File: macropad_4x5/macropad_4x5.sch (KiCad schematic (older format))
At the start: 41 parts

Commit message: Update to THT diodes
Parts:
- D1, D10, D11, D12, D13, D14, D15, D16, D17, D18, D19, D2, D20, D3, D4, D5, D6, D7, D8, D9: footprint Diode_SMD:D_SOD-123 -> Diode_THT:D_A-405_P7.62mm_Horizontal
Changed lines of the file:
@@
 F 0 "D1" H 3950 1950 50  0000 R CNN
 F 1 "D_Small" H 4100 2050 50  0000 R CNN
-F 2 "Diode_SMD:D_SOD-123" V 3900 1850 50  0001 C CNN
+F 2 "Diode_THT:D_A-405_P7.62mm_Horizontal" V 3900 1850 50  0001 C CNN
 F 3 "~" V 3900 1850 50  0001 C CNN
 	1    3900 1850
@@
 F 0 "D5" H 3950 2700 50  0000 R CNN
 F 1 "D_Small" H 4150 2800 50  0000 R CNN
-F 2 "Diode_SMD:D_SOD-123" V 3900 2600 50  0001 C CNN
+F 2 "Diode_THT:D_A-405_P7.62mm_Horizontal" V 3900 2600 50  0001 C CNN
 F 3 "~" V 3900 2600 50  0001 C CNN
 	1    3900 2600
@@
 F 0 "D9" H 3950 3450 50  0000 R CNN
 F 1 "D_Small" H 4150 3550 50  0000 R CNN
-F 2 "Diode_SMD:D_SOD-123" V 3900 3350 50  0001 C CNN
+F 2 "Diode_THT:D_A-405_P7.62mm_Horizontal" V 3900 3350 50  0001 C CNN
 F 3 "~" V 3900 3350 50  0001 C CNN
 	1    3900 3350
@@
 F 0 "D13" H 3950 4200 50  0000 R CNN
 F 1 "D_Small" H 4150 4300 50  0000 R CNN
-F 2 "Diode_SMD:D_SOD-123" V 3900 4100 50  0001 C CNN
+F 2 "Diode_THT:D_A-405_P7.62mm_Horizontal" V 3900 4100 50  0001 C CNN
 F 3 "~" V 3900 4100 50  0001 C CNN
 	1    3900 4100
@@
 F 0 "D17" H 3950 4950 50  0000 R CNN
 F 1 "D_Small" H 4150 5050 50  0000 R CNN
-F 2 "Diode_SMD:D_SOD-123" V 3900 4850 50  0001 C CNN
+F 2 "Diode_THT:D_A-405_P7.62mm_Horizontal" V 3900 4850 50  0001 C CNN
 F 3 "~" V 3900 4850 50  0001 C CNN
 	1    3900 4850
@@
 F 0 "D20" H 6950 4950 50  0000 R CNN
 F 1 "D_Small" H 7150 5050 50  0000 R CNN
-F 2 "Diode_SMD:D_SOD-123" V 6900 4850 50  0001 C CNN
+F 2 "Diode_THT:D_A-405_P7.62mm_Horizontal" V 6900 4850 50  0001 C CNN
 F 3 "~" V 6900 4850 50  0001 C CNN
 	1    6900 4850
@@
 F 0 "D19" H 5950 4950 50  0000 R CNN
 F 1 "D_Small" H 6150 5050 50  0000 R CNN
-F 2 "Diode_SMD:D_SOD-123" V 5900 4850 50  0001 C CNN
+F 2 "Diode_THT:D_A-405_P7.62mm_Horizontal" V 5900 4850 50  0001 C CNN
 F 3 "~" V 5900 4850 50  0001 C CNN
 	1    5900 4850
@@
 F 0 "D18" H 4950 4950 50  0000 R CNN
 F 1 "D_Small" H 5150 5050 50  0000 R CNN
-F 2 "Diode_SMD:D_SOD-123" V 4900 4850 50  0001 C CNN
+F 2 "Diode_THT:D_A-405_P7.62mm_Horizontal" V 4900 4850 50  0001 C CNN
 F 3 "~" V 4900 4850 50  0001 C CNN
 	1    4900 4850
@@
 F 0 "D16" H 6950 4200 50  0000 R CNN
 F 1 "D_Small" H 7150 4300 50  0000 R CNN
-F 2 "Diode_SMD:D_SOD-123" V 6900 4100 50  0001 C CNN
+F 2 "Diode_THT:D_A-405_P7.62mm_Horizontal" V 6900 4100 50  0001 C CNN
 F 3 "~" V 6900 4100 50  0001 C CNN
 	1    6900 4100
@@
 F 0 "D15" H 5950 4200 50  0000 R CNN
 F 1 "D_Small" H 6150 4300 50  0000 R CNN
-F 2 "Diode_SMD:D_SOD-123" V 5900 4100 50  0001 C CNN
+F 2 "Diode_THT:D_A-405_P7.62mm_Horizontal" V 5900 4100 50  0001 C CNN
 F 3 "~" V 5900 4100 50  0001 C CNN
 	1    5900 4100
@@
 F 0 "D14" H 4950 4200 50  0000 R CNN
 F 1 "D_Small" H 5150 4300 50  0000 R CNN
-F 2 "Diode_SMD:D_SOD-123" V 4900 4100 50  0001 C CNN
+F 2 "Diode_THT:D_A-405_P7.62mm_Horizontal" V 4900 4100 50  0001 C CNN
 F 3 "~" V 4900 4100 50  0001 C CNN
 	1    4900 4100
@@
 F 0 "D12" H 6950 3450 50  0000 R CNN
 F 1 "D_Small" H 7150 3550 50  0000 R CNN
-F 2 "Diode_SMD:D_SOD-123" V 6900 3350 50  0001 C CNN
+F 2 "Diode_THT:D_A-405_P7.62mm_Horizontal" V 6900 3350 50  0001 C CNN
 F 3 "~" V 6900 3350 50  0001 C CNN
 	1    6900 3350
@@
 F 0 "D11" H 5950 3450 50  0000 R CNN
 F 1 "D_Small" H 6150 3550 50  0000 R CNN
-F 2 "Diode_SMD:D_SOD-123" V 5900 3350 50  0001 C CNN
+F 2 "Diode_THT:D_A-405_P7.62mm_Horizontal" V 5900 3350 50  0001 C CNN
 F 3 "~" V 5900 3350 50  0001 C CNN
 	1    5900 3350
@@
 F 0 "D10" H 4950 3450 50  0000 R CNN
 F 1 "D_Small" H 5150 3550 50  0000 R CNN
-F 2 "Diode_SMD:D_SOD-123" V 4900 3350 50  0001 C CNN
+F 2 "Diode_THT:D_A-405_P7.62mm_Horizontal" V 4900 3350 50  0001 C CNN
 F 3 "~" V 4900 3350 50  0001 C CNN
 	1    4900 3350
@@
 F 0 "D8" H 6950 2700 50  0000 R CNN
 F 1 "D_Small" H 7150 2800 50  0000 R CNN
-F 2 "Diode_SMD:D_SOD-123" V 6900 2600 50  0001 C CNN
+F 2 "Diode_THT:D_A-405_P7.62mm_Horizontal" V 6900 2600 50  0001 C CNN
 F 3 "~" V 6900 2600 50  0001 C CNN
 	1    6900 2600
@@
 F 0 "D7" H 5950 2700 50  0000 R CNN
 F 1 "D_Small" H 6150 2800 50  0000 R CNN
-F 2 "Diode_SMD:D_SOD-123" V 5900 2600 50  0001 C CNN
+F 2 "Diode_THT:D_A-405_P7.62mm_Horizontal" V 5900 2600 50  0001 C CNN
 F 3 "~" V 5900 2600 50  0001 C CNN
 	1    5900 2600
@@
 F 0 "D6" H 4950 2700 50  0000 R CNN
 F 1 "D_Small" H 5150 2800 50  0000 R CNN
-F 2 "Diode_SMD:D_SOD-123" V 4900 2600 50  0001 C CNN
+F 2 "Diode_THT:D_A-405_P7.62mm_Horizontal" V 4900 2600 50  0001 C CNN
 F 3 "~" V 4900 2600 50  0001 C CNN
 	1    4900 2600
@@
 F 0 "D4" H 6950 1950 50  0000 R CNN
 F 1 "D_Small" H 7150 2050 50  0000 R CNN
-F 2 "Diode_SMD:D_SOD-123" V 6900 1850 50  0001 C CNN
+F 2 "Diode_THT:D_A-405_P7.62mm_Horizontal" V 6900 1850 50  0001 C CNN
 F 3 "~" V 6900 1850 50  0001 C CNN
 	1    6900 1850
@@
 F 0 "D3" H 5950 1950 50  0000 R CNN
 F 1 "D_Small" H 6150 2050 50  0000 R CNN
-F 2 "Diode_SMD:D_SOD-123" V 5900 1850 50  0001 C CNN
+F 2 "Diode_THT:D_A-405_P7.62mm_Horizontal" V 5900 1850 50  0001 C CNN
 F 3 "~" V 5900 1850 50  0001 C CNN
 	1    5900 1850
@@
 F 0 "D2" H 4950 1950 50  0000 R CNN
 F 1 "D_Small" H 5100 2050 50  0000 R CNN
-F 2 "Diode_SMD:D_SOD-123" V 4900 1850 50  0001 C CNN
+F 2 "Diode_THT:D_A-405_P7.62mm_Horizontal" V 4900 1850 50  0001 C CNN
 F 3 "~" V 4900 1850 50  0001 C CNN
 	1    4900 1850

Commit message: Updated schematic and pcb routing
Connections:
- net col0: now also B1.20 (A3); no longer B1.17 (A0)
- net col1: now also B1.19 (A2); no longer B1.18 (A1)
- net col2: now also B1.17 (A0); no longer B1.19 (A2)
- net col3: now also B1.18 (A1); no longer B1.20 (A3)
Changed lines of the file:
@@
 Text GLabel 3450 4950 0    50   Input ~ 0
 row4
+Text GLabel 2100 3100 2    50   Input ~ 0
+col0
+Text GLabel 2100 3200 2    50   Input ~ 0
+col1
 Text GLabel 2100 3400 2    50   Input ~ 0
-col0
+col2
 Text GLabel 2100 3300 2    50   Input ~ 0
-col1
-Text GLabel 2100 3200 2    50   Input ~ 0
-col2
-Text GLabel 2100 3100 2    50   Input ~ 0
 col3
 Text GLabel 1200 3100 0    50   Input ~ 0

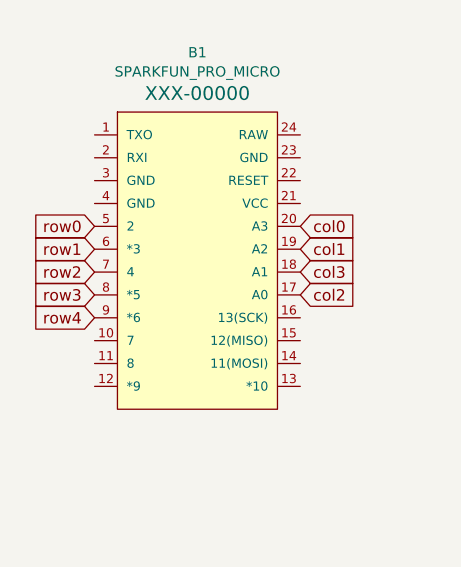
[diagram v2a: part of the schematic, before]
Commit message: Updated schematics and pcb design to clean it up
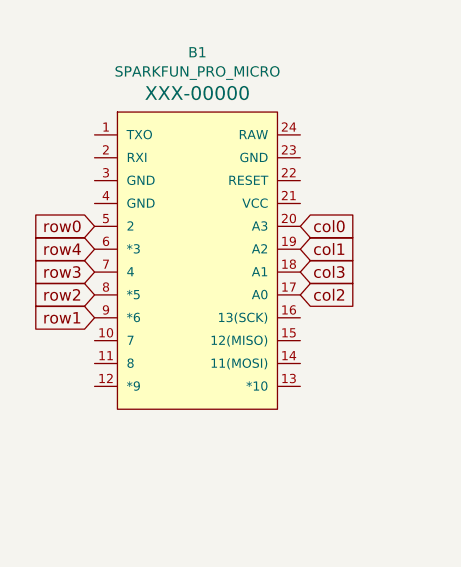
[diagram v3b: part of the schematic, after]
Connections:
- net row1: now also B1.9 (*6); no longer B1.6 (*3)
- net row2: now also B1.8 (*5); no longer B1.7 (4)
- net row3: now also B1.7 (4); no longer B1.8 (*5)
- net row4: now also B1.6 (*3); no longer B1.9 (*6)
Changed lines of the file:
@@
 Text GLabel 1200 3100 0    50   Input ~ 0
 row0
+Text GLabel 1200 3500 0    50   Input ~ 0
+row1
+Text GLabel 1200 3400 0    50   Input ~ 0
+row2
+Text GLabel 1200 3300 0    50   Input ~ 0
+row3
 Text GLabel 1200 3200 0    50   Input ~ 0
-row1
-Text GLabel 1200 3300 0    50   Input ~ 0
-row2
-Text GLabel 1200 3400 0    50   Input ~ 0
-row3
-Text GLabel 1200 3500 0    50   Input ~ 0
 row4
 $EndSCHEMATC

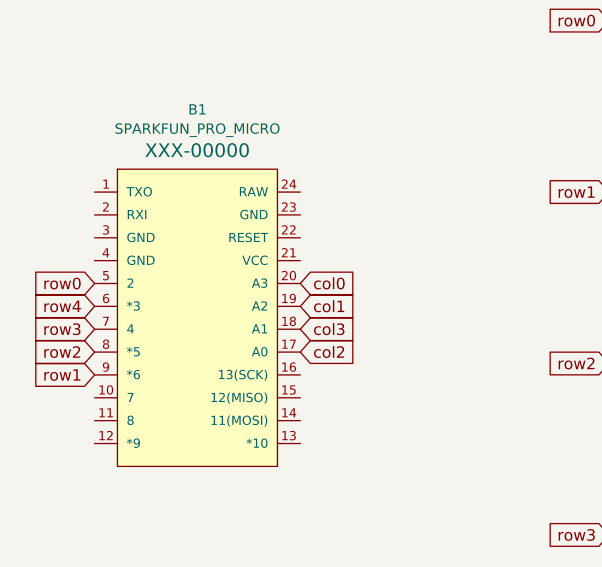
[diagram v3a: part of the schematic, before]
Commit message: Updated PCB
The pro micro was facing the wrong way previously. Also added more text
to the silk layers to help marking for use.
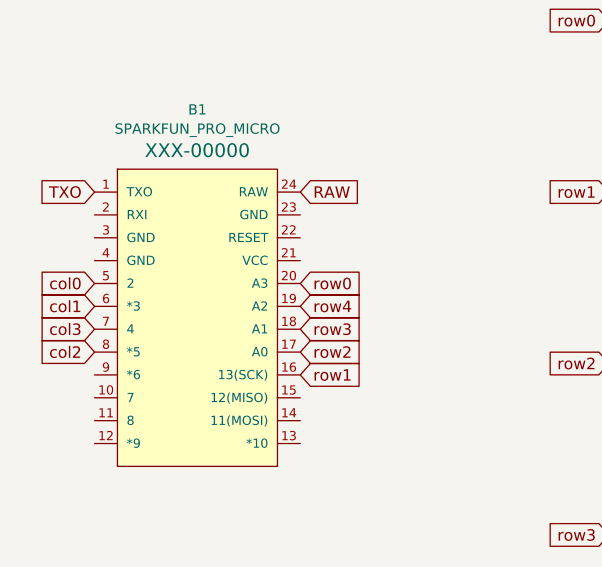
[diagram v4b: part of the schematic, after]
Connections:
- net col0: now also B1.5 (2); no longer B1.20 (A3)
- net col1: now also B1.6 (*3); no longer B1.19 (A2)
- net col2: now also B1.8 (*5); no longer B1.17 (A0)
- net col3: now also B1.7 (4); no longer B1.18 (A1)
- net row0: now also B1.20 (A3); no longer B1.5 (2)
- net row1: now also B1.16 (13(SCK)); no longer B1.9 (*6)
- net row2: now also B1.17 (A0); no longer B1.8 (*5)
- net row3: now also B1.18 (A1); no longer B1.7 (4)
- net row4: now also B1.19 (A2); no longer B1.6 (*3)
- net TXO: now reaches B1.1 (TXO)
- net RAW: now reaches B1.24 (RAW)
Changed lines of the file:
@@
 Text GLabel 3450 4950 0    50   Input ~ 0
 row4
+Text GLabel 1200 3100 0    50   Input ~ 0
+col0
+Text GLabel 1200 3200 0    50   Input ~ 0
+col1
+Text GLabel 1200 3400 0    50   Input ~ 0
+col2
+Text GLabel 1200 3300 0    50   Input ~ 0
+col3
 Text GLabel 2100 3100 2    50   Input ~ 0
-col0
+row0
+Text GLabel 2100 3500 2    50   Input ~ 0
+row1
+Text GLabel 2100 3400 2    50   Input ~ 0
+row2
+Text GLabel 2100 3300 2    50   Input ~ 0
+row3
 Text GLabel 2100 3200 2    50   Input ~ 0
-col1
-Text GLabel 2100 3400 2    50   Input ~ 0
-col2
-Text GLabel 2100 3300 2    50   Input ~ 0
-col3
-Text GLabel 1200 3100 0    50   Input ~ 0
-row0
-Text GLabel 1200 3500 0    50   Input ~ 0
-row1
-Text GLabel 1200 3400 0    50   Input ~ 0
-row2
-Text GLabel 1200 3300 0    50   Input ~ 0
-row3
-Text GLabel 1200 3200 0    50   Input ~ 0
 row4
+Text GLabel 2100 2700 2    50   Input ~ 0
+RAW
+Text GLabel 1200 2700 0    50   Input ~ 0
+TXO
 $EndSCHEMATC

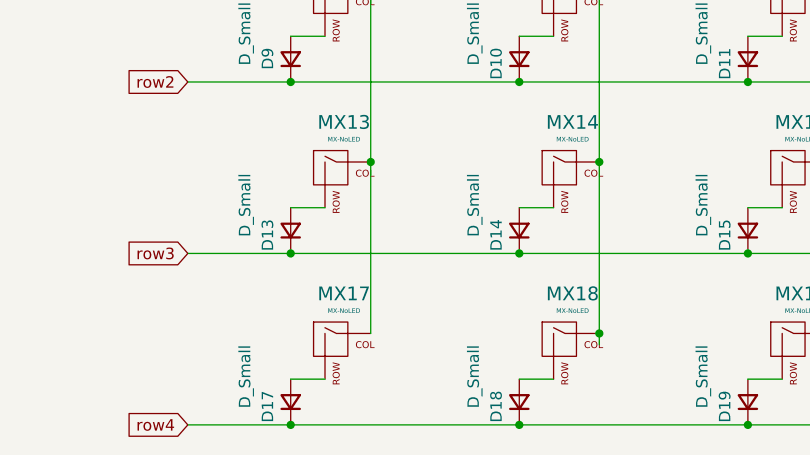
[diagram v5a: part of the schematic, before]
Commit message: Minor updates to 4x5 macropad files
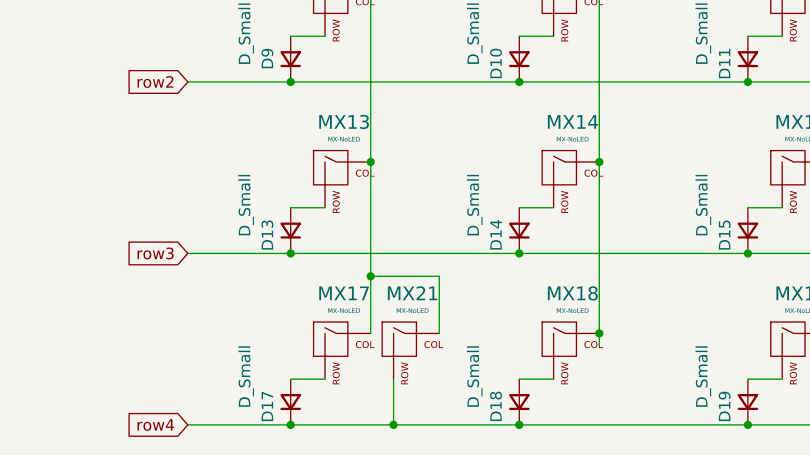
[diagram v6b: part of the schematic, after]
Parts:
- added MX21: MX-NoLED, MX_Alps_Hybrid:MX-2U-ReversedStabilizers-NoLED, symbol MX_Alps_Hybrid:MX-NoLED
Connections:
- net col0: now also MX21.1 (COL)
- net row4: now also MX21.2 (ROW)
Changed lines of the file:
@@
 $EndComp
 Wire Wire Line
-	4250 4550 4250 3800
+	4250 4550 4250 4300
 Wire Wire Line
 	4250 3800 4250 3050
@@
 Connection ~ 4900 4950
 Wire Wire Line
-	4900 4950 3900 4950
+	4900 4950 4350 4950
 Connection ~ 5900 4950
 Wire Wire Line
@@
 Text GLabel 1200 2700 0    50   Input ~ 0
 TXO
+$Comp
+L MX_Alps_Hybrid:MX-NoLED MX21
+U 1 1 5FDEFDC1
+P 4400 4600
+F 0 "MX21" H 4433 4823 60  0000 C CNN
+F 1 "MX-NoLED" H 4433 4749 20  0000 C CNN
+F 2 "MX_Alps_Hybrid:MX-2U-ReversedStabilizers-NoLED" H 3775 4575 60  0001 C CNN
+F 3 "" H 3775 4575 60  0001 C CNN
+	1    4400 4600
+	1    0    0    -1
+$EndComp
+Wire Wire Line
+	4250 4300 4550 4300
+Wire Wire Line
+	4550 4300 4550 4550
+Connection ~ 4250 4300
+Wire Wire Line
+	4250 4300 4250 3800
+Wire Wire Line
+	4350 4750 4350 4950
+Connection ~ 4350 4950
+Wire Wire Line
+	4350 4950 3900 4950
 $EndSCHEMATC
